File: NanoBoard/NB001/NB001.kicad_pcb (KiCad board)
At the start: 2 copper layers, 22 x 72.8 mm, 18 parts, among them M1 Motor_DC, SW1 SW, SW2 Limit Switch, U2 MS583730BA01-50, U4 XiaoESP32C3

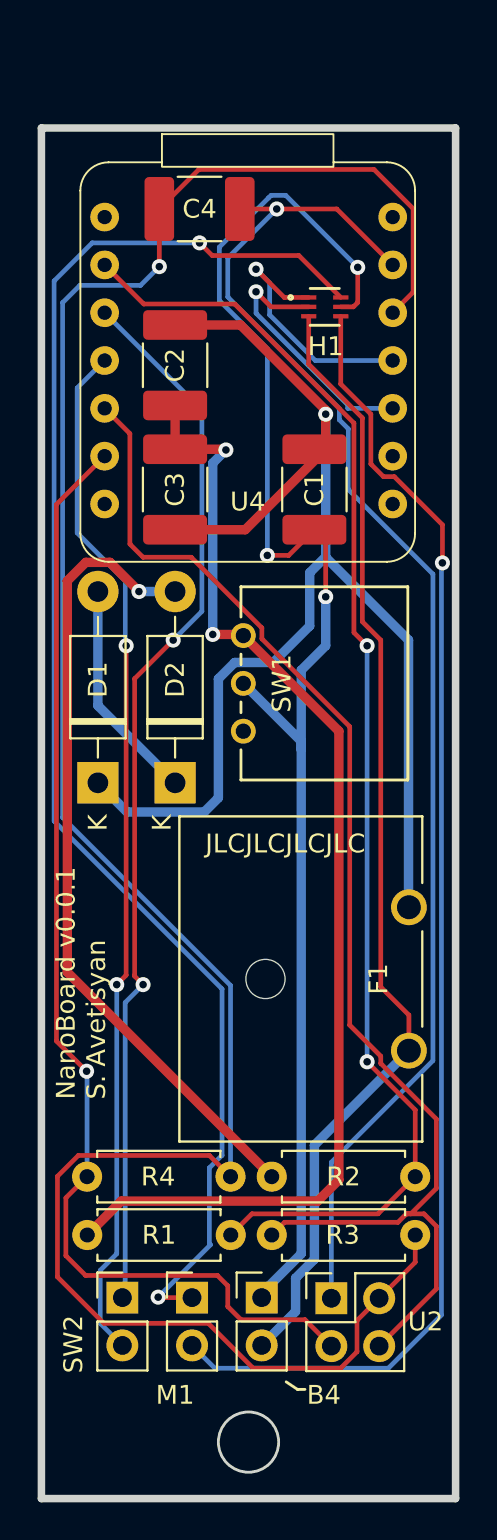
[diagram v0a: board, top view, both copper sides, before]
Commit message: Restructuring the Directories and Naming Conventions
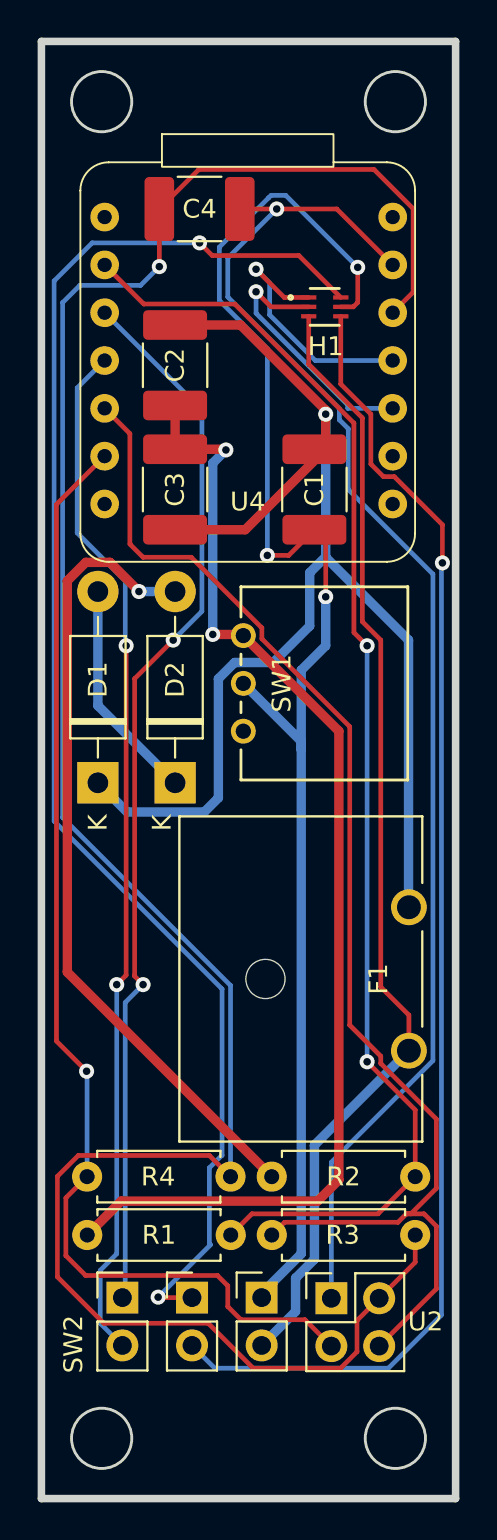
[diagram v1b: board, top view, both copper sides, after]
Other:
- board size 22 x 72.8 mm -> 22 x 77.4 mm
- board text removed: "JLCJLCJLCJLC"
- board text removed: "NanoBoard v0.0.1 S. Avetisyan"
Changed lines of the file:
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@@
     (property "ki_keywords" "battery cell")
     (attr through_hole)
-    (fp_text reference "B4" (at 3.3 5.175) (layer "F.SilkS")
+    (fp_text reference "B4" (at -0.5 -2.025) (layer "F.SilkS") hide
         (effects (font (size 1 1) (thickness 0.15)))
     )
@@
     (property "ki_keywords" "DC Motor")
     (attr through_hole)
-    (fp_text reference "M1" (at -0.9 5.175) (layer "F.SilkS")
+    (fp_text reference "M1" (at 0 -2.33) (layer "F.SilkS") hide
         (effects (font (size 1 1) (thickness 0.15)))
     )
@@
     )
   )
-  (gr_line (start 128.2 140.1) (end 127.6 139.7)
-    (stroke (width 0.15) (type default)) (layer "F.SilkS"))
-  (gr_line (start 128.6 140.1) (end 128.2 140.1)
-    (stroke (width 0.15) (type default)) (layer "F.SilkS"))
-  (gr_circle (center 125.6 142.9) (end 128.6 142.9)
+  (gr_circle (center 133.4 142.7) (end 136.4 142.7)
     (stroke (width 0.1) (type dot)) (fill none) (layer "Dwgs.User"))
-  (gr_rect (start 114.6 73.1) (end 136.6 145.9)
+  (gr_circle (center 117.8 142.7) (end 120.8 142.7)
+    (stroke (width 0.1) (type dot)) (fill none) (layer "Dwgs.User"))
+  (gr_circle (center 117.8 71.7) (end 120.8 71.7)
+    (stroke (width 0.1) (type dot)) (fill none) (layer "Dwgs.User"))
+  (gr_circle (center 133.4 71.7) (end 136.4 71.7)
+    (stroke (width 0.1) (type dot)) (fill none) (layer "Dwgs.User"))
+  (gr_rect (start 114.6 68.5) (end 136.6 145.9)
     (stroke (width 0.4) (type default)) (fill none) (layer "Edge.Cuts"))
-  (gr_circle (center 125.6 142.9) (end 127.2 142.9)
+  (gr_circle (center 133.4 71.7) (end 135 71.7)
     (stroke (width 0.15) (type default)) (fill none) (layer "Edge.Cuts"))
-  (gr_text "NanoBoard v0.0.1\nS. Avetisyan" (at 118.1 111.2 90) (layer "B.SilkS")
-    (effects (font (size 1 1) (thickness 0.15)) (justify left bottom mirror))
-  )
-  (gr_text "NanoBoard v0.0.1\nS. Avetisyan" (at 118.1 124.7 90) (layer "F.SilkS")
-    (effects (font (size 1 1) (thickness 0.15)) (justify left bottom))
-  )
-  (gr_text "JLCJLCJLCJLC" (at 123.3 111.7) (layer "F.SilkS")
-    (effects (font (size 1 1) (thickness 0.15)) (justify left bottom))
+  (gr_circle (center 117.8 142.7) (end 119.4 142.7)
+    (stroke (width 0.15) (type default)) (fill none) (layer "Edge.Cuts"))
+  (gr_circle (center 117.8 71.7) (end 119.4 71.7)
+    (stroke (width 0.15) (type default)) (fill none) (layer "Edge.Cuts"))
+  (gr_circle (center 133.4 142.7) (end 135 142.7)
+    (stroke (width 0.15) (type default)) (fill none) (layer "Edge.Cuts"))
+  (dimension (type aligned) (layer "Dwgs.User")
+    (pts (xy 114.6 68.5) (xy 136.6 68.5))
+    (height -1.6)
+    (gr_text "22.0000 mm" (at 125.6 65.75) (layer "Dwgs.User")
+      (effects (font (size 1 1) (thickness 0.15)))
+    )
+    (format (prefix "") (suffix "") (units 3) (units_format 1) (precision 4))
+    (style (thickness 0.1) (arrow_length 1.27) (text_position_mode 0) (extension_height 0.58642) (extension_offset 0.5) keep_text_aligned)
+  )
+  (dimension (type aligned) (layer "Dwgs.User")
+    (pts (xy 136.6 68.5) (xy 136.6 145.9))
+    (height -3.7)
+    (gr_text "77.4000 mm" (at 139.15 107.2 90) (layer "Dwgs.User")
+      (effects (font (size 1 1) (thickness 0.15)))
+    )
+    (format (prefix "") (suffix "") (units 3) (units_format 1) (precision 4))
+    (style (thickness 0.1) (arrow_length 1.27) (text_position_mode 0) (extension_height 0.58642) (extension_offset 0.5) keep_text_aligned)
   )
   (segment (start 129.1 94.4375) (end 127.7375 95.8) (width 0.25) (layer "F.Cu") (net 1))
